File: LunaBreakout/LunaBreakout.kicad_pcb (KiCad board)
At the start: 2 copper layers, 78.5 x 59.4 mm, 62 parts, among them J1 Conn_01x03, J10 Conn_01x02, J11 Conn_01x03, J12 Conn_01x03, J13 Conn_01x04, J14 Conn_01x04, J15 5 V BEC, J16 GND, J17 Conn_01x04, J18 Conn_01x04, J19 Conn_01x04, J2 Conn_01x03, J3 Conn_01x04, J4 Conn_01x03, J5 Conn_01x03, J6 USB_C_Receptacle_USB2.0_16P, J8 Conn_01x04, J9 Conn_01x04, SW1 SW_SPST, U1 RP2040, U2 AMS1117-3.3, U3 W25Q32JVSS, U4 ISO7721D, U5 ISO7720D, U8 ISO7741DBQ, Y1 12Mhz

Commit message: Added labels on front silkscreen for connectors, designating connector function
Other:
- board text added: "ADC0"
- board text added: "ADC1"
- board text added: "ADC2"
- board text added: "ADC3"
- board text added: "SCL0"
- board text added: "SCL1"
- board text added: "SDA0"
- board text added: "SDA1"
- board text added: "SPI0CS0"
- board text added: "SPI0CS1"
- board text added: "SPI0CS2"
- board text added: "SPI0RX"
- board text added: "SPI0SCLK"
- board text added: "SPI0TX"
- board text added: "SPI1CS0"
- board text added: "SPI1CS1"
- board text added: "SPI1CS2"
- board text added: "SPI1RX"
- board text added: "SPI1SCLK"
- board text added: "SPI1TX"
- board text added: "UART0RX"
- board text added: "UART0TX"
- board text added: "UART1RX"
- board text added: "UART1TX"

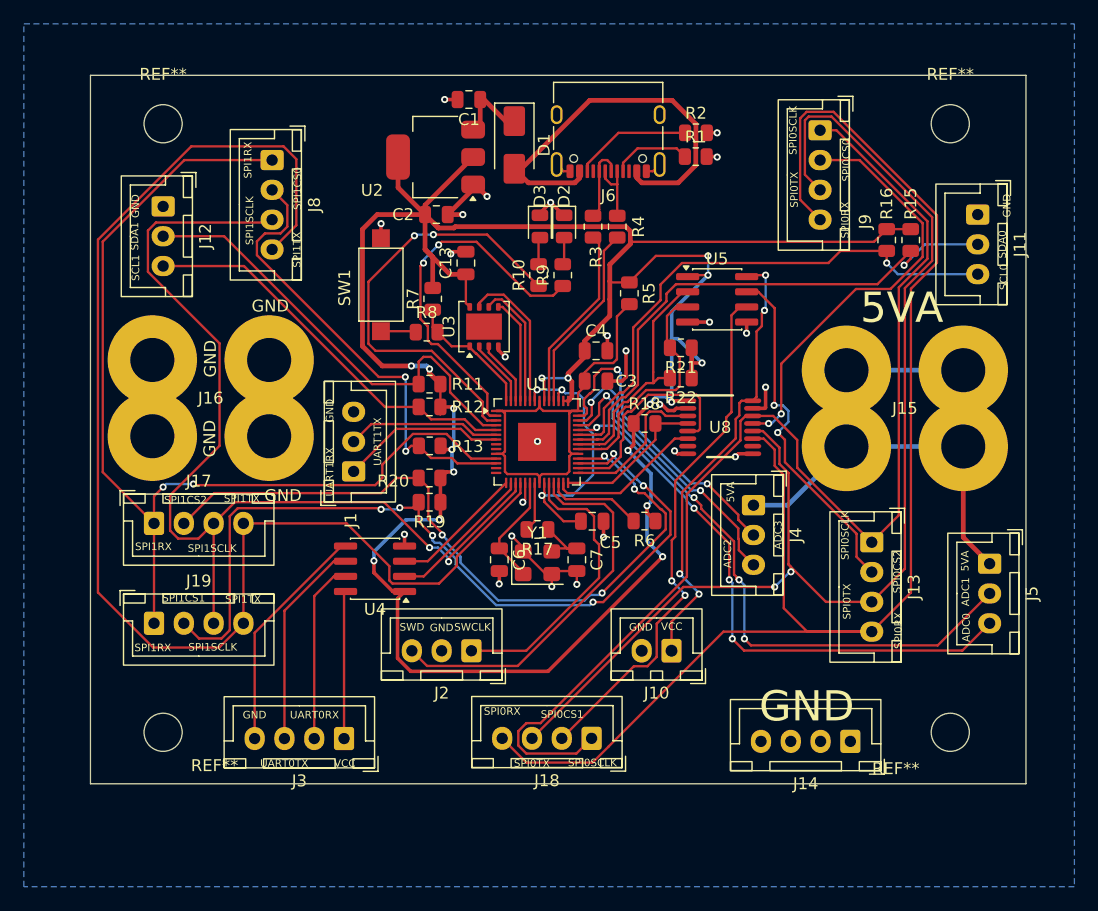
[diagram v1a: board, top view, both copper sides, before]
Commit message: Moved labels, will need to resize all of them and look into making board bigger so we can have labels
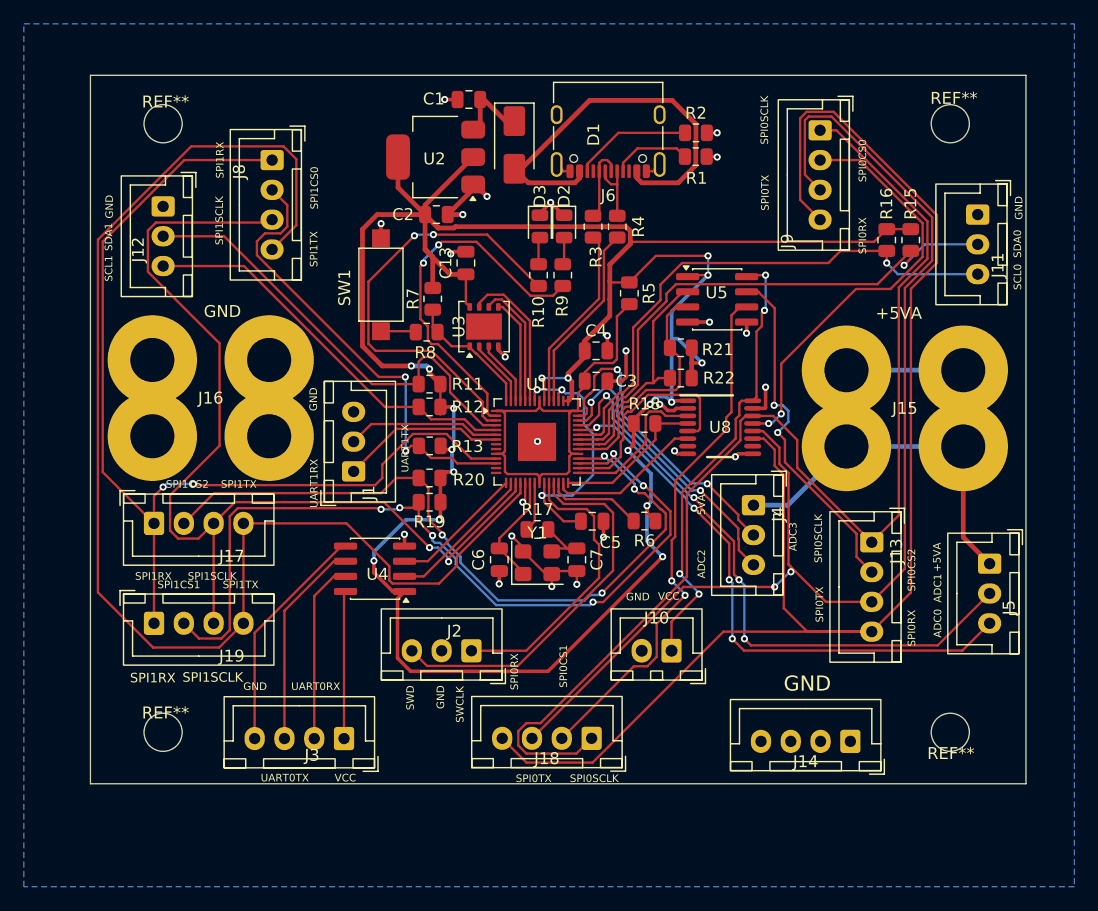
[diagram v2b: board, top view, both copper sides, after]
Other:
- board text added: "+5VA"
